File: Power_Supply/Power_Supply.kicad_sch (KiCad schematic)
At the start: 2 parts, among them T1 FL+30_18

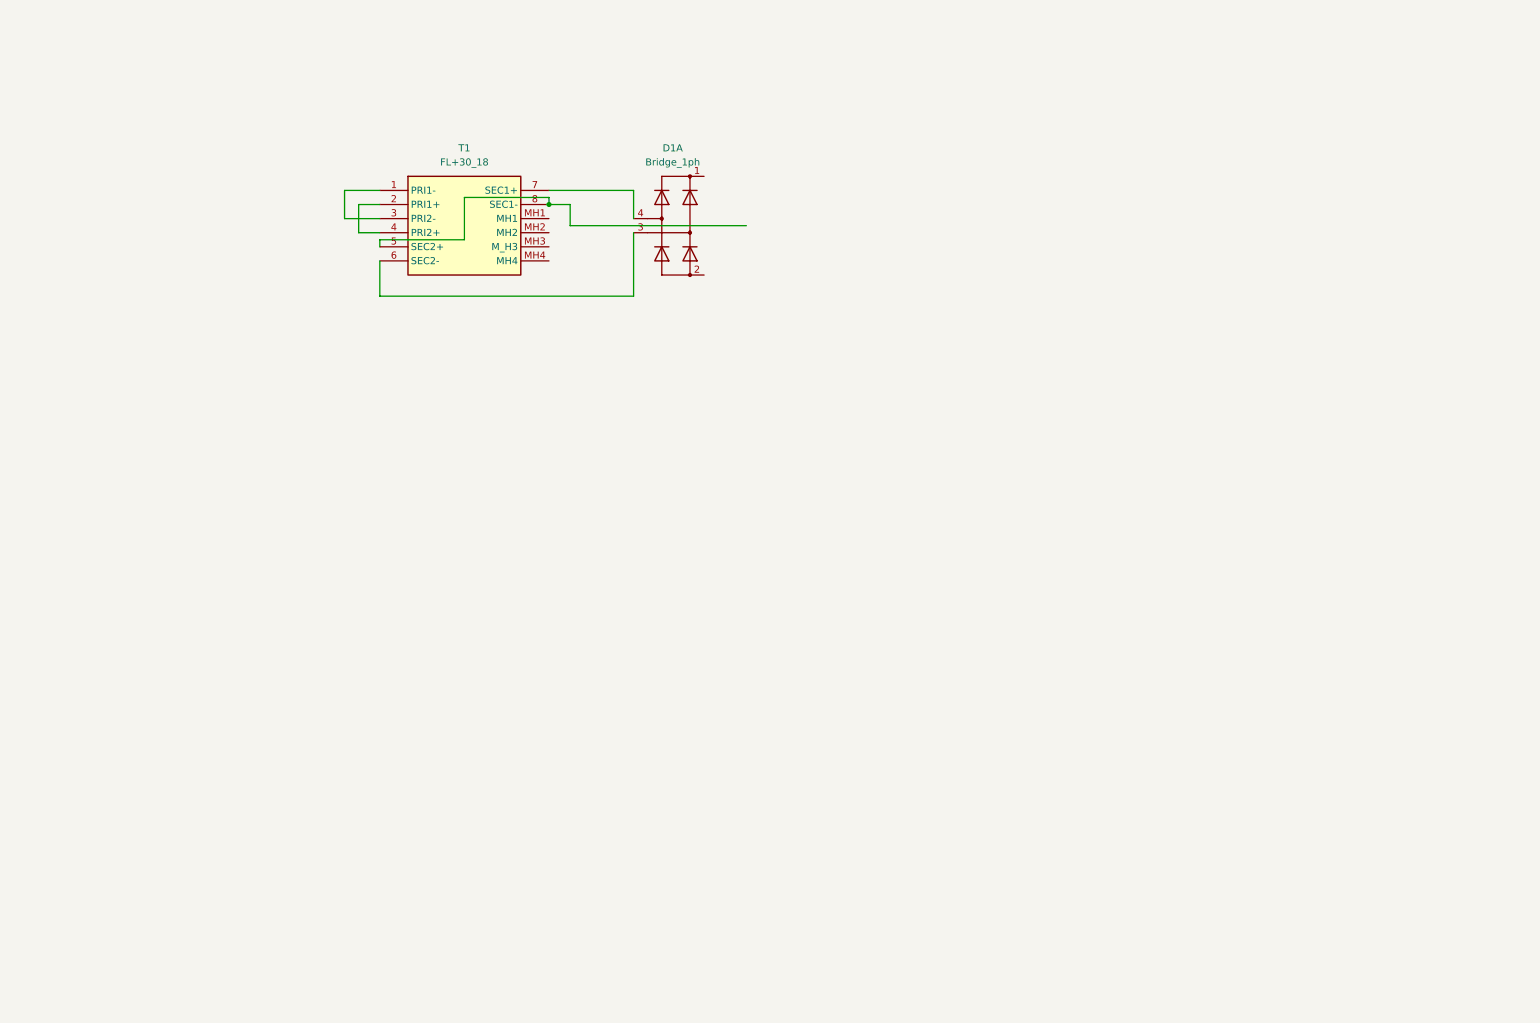
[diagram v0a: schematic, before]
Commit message: updates to Spice Model, Power Supply Design
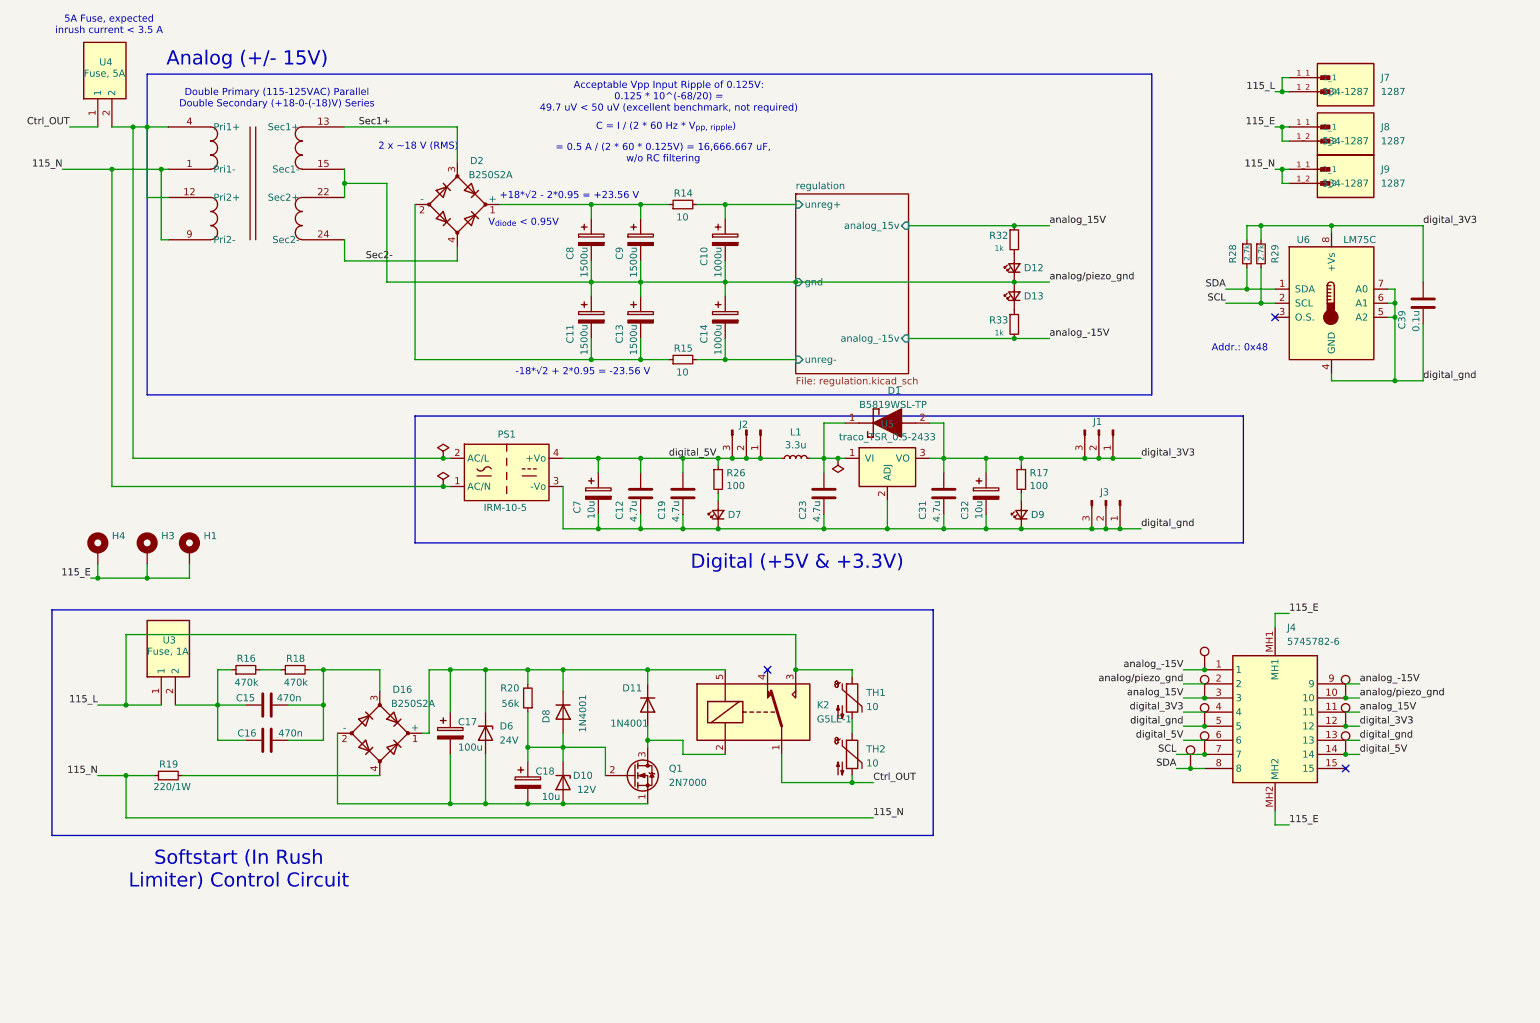
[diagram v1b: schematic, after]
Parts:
- removed D1: Bridge_1ph, B250SA_SLIM:P20_SO-DIL-Slim, symbol bridge_1ph:Bridge_1ph
- removed T1: FL+30_18, FL3018:FL3018, symbol FL+30_18:FL+30_18
- added C10, C14: 1000u, CP_Radial_D12.5mm_P5.00mm_+Better, symbol Supply-Board-rescue:CP-Device
- added C11, C13, C8, C9: 1500u, CP_Radial_D12.5mm_P5.00mm_+Better, symbol Supply-Board-rescue:CP-Device
- added C12, C19, C23, C31: 4.7u, Capacitor_SMD:C_0603_1608Metric, symbol Device:C
- added C15, C16: 470n, X2_470n:CAP_R46KN347000N0M_KEM, symbol Device:C
- added C17: 100u, Capacitor_THT:C_Radial_D10.0mm_H12.5mm_P5.00mm, symbol Supply-Board-rescue:CP-Device
- added C18: 10u, Capacitor_THT:CP_Radial_D5.0mm_P2.00mm, symbol Supply-Board-rescue:CP-Device
- added C32, C7: 10u, Capacitor_Tantalum_SMD:CP_EIA-7343-31_Kemet-D, symbol Supply-Board-rescue:CP-Device
- added C39: 0.1u, Capacitor_SMD:C_0603_1608Metric, symbol Device:C
- added D1: B5819WSL-TP, B5819WSL-TP:SODFL2512X90N, symbol B5819WSL-TP:B5819WSL-TP
- added D10: 12V, Diode_SMD:D_SOD-123, symbol Device:D_Zener
- added D11, D8: 1N4001, Diode_THT:D_DO-41_SOD81_P10.16mm_Horizontal, symbol Diode:1N4001
- added D12, D13, D7, D9: LED_Small, LED_SMD:LED_0603_1608Metric, symbol Device:LED_Small
- added D16, D2: B250S2A, B250SA_SLIM:P20_SO-DIL-Slim, symbol Device:D_Bridge_+-AA
- added D6: 24V, Diode_SMD:D_SOD-123, symbol Device:D_Zener
- added H1, H3, H4: MountingHole_Pad, MountingHole:MountingHole_3.2mm_M3_Pad_Via, symbol Mechanical:MountingHole_Pad
- added J1, J2, J3: Conn_01x03_Pin, Connector_PinHeader_2.54mm:PinHeader_1x03_P2.54mm_Vertical, symbol Connector:Conn_01x03_Pin
- added J4: 5745782-6, 57457826:57457826, symbol 5745782-6:5745782-6
- added J7, J8, J9: 1287, 1287:KEYSTONE_1287, symbol 1287:1287
- added K2: G5LE-1, Relay_THT:Relay_SPDT_Omron-G5LE-1, symbol Relay:G5LE-1
- added L1: 3.3u, SRR1280_3R3Y:IND_BOURNS_SRR1280, symbol Device:L_Small
- added PS1: IRM-10-5, Converter_ACDC:Converter_ACDC_MeanWell_IRM-10-xx_THT, symbol Converter_ACDC:IRM-10-5
- added Q1: 2N7000, Package_TO_SOT_THT:TO-92_Inline, symbol Transistor_FET:2N7000
- added R14, R15: 10, Resistor_SMD:R_1206_3216Metric, symbol Device:R_Small
- added R16, R18: 470k, Resistor_THT:R_Axial_DIN0207_L6.3mm_D2.5mm_P15.24mm_Horizontal, symbol Device:R_Small
- added R17, R26: 100, Resistor_SMD:R_0805_2012Metric, symbol Device:R_Small
- added R19: 220/1W, Resistor_SMD:R_2512_6332Metric, symbol Device:R_Small
- added R20: 56k, Resistor_SMD:R_0805_2012Metric, symbol Device:R_Small
- added R28, R29: 2.7k, Resistor_SMD:R_0805_2012Metric, symbol Device:R_Small
- added R32, R33: 1k, Resistor_SMD:R_0805_2012Metric, symbol Device:R_Small
- added T1: ~, FLN_40_18:FLN_40_18, symbol FLN_40_18:FLN_40_18
- added TH1, TH2: 10, Resistor_THT:R_Axial_DIN0204_L3.6mm_D1.6mm_P5.08mm_Horizontal, symbol Device:Thermistor_NTC
- added TP1, TP2, TP3, TP4, TP5, TP6, TP7, TP8: TestPoint, TestPoint:TestPoint_Loop_D1.80mm_Drill1.0mm_Beaded, symbol Connector:TestPoint
- added U3: Fuse, 1A, LittleFuseHolder5x20mm:0PTF0078P, symbol 0PTF0078P:0PTF0078P
- added U4: Fuse, 5A, LittleFuseHolder5x20mm:0PTF0078P, symbol 0PTF0078P:0PTF0078P
- added U5: traco_TSR_0.5-2433, TSR-0.5-2433:TSR-0.5-2433, symbol Supply-Board-rescue:traco_TSR_0.5-2433-STM_Custom_Lib
- added U6: LM75C, Package_SO:SOIC-8_3.9x4.9mm_P1.27mm, symbol Supply-Board-rescue:LM75C-Sensor_Temperature
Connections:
- new net: D7.2 (A), R26.2
- new net: D9.2 (A), R17.2
- new net: C23.1, D1.1 (K), L1.2, U5.1 (VI)
- new net: D13.1 (K), R33.1
- new net: C17.1, D11.1 (K), D16.1 (+), D6.1 (K), D8.1 (K), K2.5, R20.2
- new net: C17.2, C18.2, D10.2 (A), D16.2 (-), D6.2 (A), Q1.1 (S)
- new net: C15.2, C16.2, D16.3, R18.2
- new net: D16.4, R19.2
- new net: TH1.2, TH2.1
- new net: C15.1, C16.1, R16.1, U3.2
- new net: C8.1, C9.1, D2.1 (+), R14.1
- new net: C11.2, C13.2, D2.2 (-), R15.1
- new net: C18.1, D10.1 (K), D8.2 (A), Q1.2 (G), R20.1
- new net: D11.2 (A), K2.2, Q1.3 (D)
- new net: D12.2 (A), R32.2
- new net: R16.2, R18.1
- new net: PS1.2 (AC/L), T1.12 (Pri2+), T1.4 (Pri1+), U4.2
- new net 115_E: H1.1, H3.1, H4.1, J4.MH1, J4.MH2, J8.1_1, J8.1_2
- new net 115_L: J7.1_1, J7.1_2, K2.3, TH1.1, U3.1
- new net 115_N: J9.1_1, J9.1_2, PS1.1 (AC/N), R19.1, T1.1 (Pri1-), T1.9 (Pri2-)
- new net Ctrl_OUT: K2.1, TH2.2, U4.1
- new net SCL: J4.7, R29.2, TP7.1, U6.2 (SCL)
- new net SDA: J4.8, R28.2, TP8.1, U6.1 (SDA)
- new net Sec1+: D2.3, T1.13 (Sec1+)
- new net Sec2-: D2.4, T1.24 (Sec2-)
- new net analog_-15V: J4.1, J4.9, R33.2, TP1.1
- new net analog_15V: J4.11, J4.3, R32.1, TP3.1
- new net analog/piezo_gnd: C10.2, C11.1, C13.1, C14.1, C8.2, C9.2, D12.1 (K), D13.2 (A), J4.10, J4.2, T1.15 (Sec1-), T1.22 (Sec2+), TP2.1
- new net digital_3V3: C31.1, C32.1, C39.1, D1.2 (A), J1.1 (Pin_1), J1.2 (Pin_2), J1.3 (Pin_3), J4.12, J4.4, R17.1, R28.1, R29.1, TP4.1, U5.3 (VO), U6.8 (+Vs)
- new net digital_5V: C12.1, C19.1, C7.1, J2.1 (Pin_1), J2.2 (Pin_2), J2.3 (Pin_3), J4.14, J4.6, L1.1, PS1.4 (+Vo), R26.1, TP6.1
- new net digital_gnd: C12.2, C19.2, C23.2, C31.2, C32.2, C39.2, C7.2, D7.1 (K), D9.1 (K), J3.1 (Pin_1), J3.2 (Pin_2), J3.3 (Pin_3), J4.13, J4.5, PS1.3 (-Vo), TP5.1, U5.2 (ADJ), U6.4 (GND), U6.5 (A2), U6.6 (A1), U6.7 (A0)
- new net regulation/unreg+: C10.1, R14.2
- new net regulation/unreg-: C14.2, R15.2
- no-connect marks 0 -> 3
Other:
- added sheet regulation (regulation.kicad_sch)
- note added: "+18*√2 - 2*0.95 = +23.56 V"
- note added: "-18*√2 + 2*0.95 = -23.56 V"
- note added: "2 x ~18 V (RMS)"
- note added: "5A Fuse, expected inrush current < 3.5 A"
- note added: "= 0.5 A / (2 * 60 * 0.125V) = 16,666.667 uF, w/o RC filtering"
- note added: "Acceptable Vpp Input Ripple of 0.125V: 0.125 * 10^(-68/20) = 49.7 uV < 50 uV (excellent benchmark, not required)"
- note added: "Addr.: 0x48"
- note added: "Analog (+/- 15V)"
- note added: "C = I / (2 * 60 Hz * V_{pp, ripple})"
- note added: "Digital (+5V & +3.3V)"
- note added: "Double Primary (115-125VAC) Parallel Double Secondary (+18-0-(-18)V) Series"
- note added: "Softstart (In Rush Limiter) Control Circuit"
- note added: "V_{diode} < 0.95V"

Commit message: Analog Circuit V1.0
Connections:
- net SCL renamed PS_Temp_SCL
- net SDA renamed PS_Temp_SDA
- net analog/piezo_gnd renamed analog_gnd
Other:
- note added: "AC Quick Connect"
- note added: "Dsub 9 Output"
- note added: "Temp Sensor"
- moved on the sheet: C15, C16, C17, C18, C39, D10, D11, D16, D6, D8, H1, H3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
